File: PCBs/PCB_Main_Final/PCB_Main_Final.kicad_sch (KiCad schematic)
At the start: 0 parts

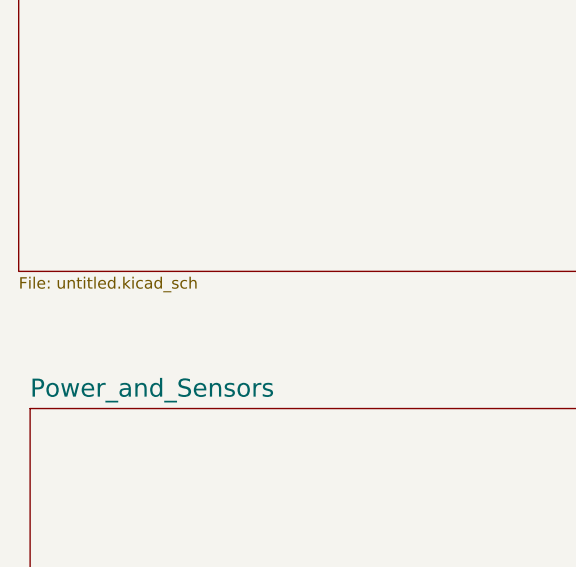
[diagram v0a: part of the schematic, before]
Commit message: fixed vias and expanded boost converter
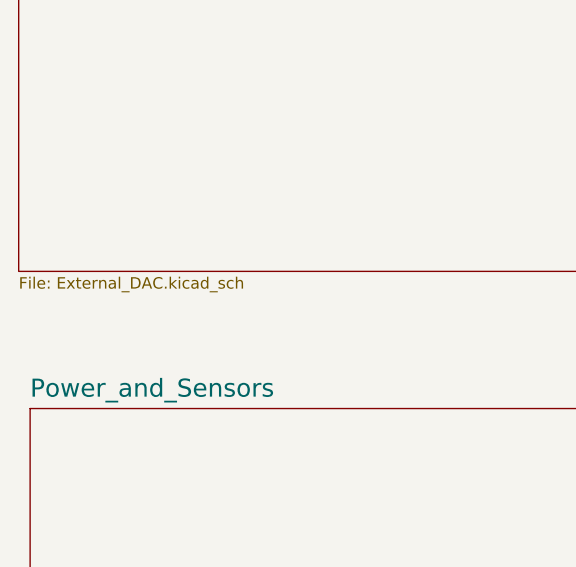
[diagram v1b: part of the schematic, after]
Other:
- sheet External_DAC: file untitled.kicad_sch -> External_DAC.kicad_sch
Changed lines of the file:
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@@
       (effects (font (size 2 2)) (justify left bottom))
     )
-    (property "Sheetfile" "untitled.kicad_sch" (at 41.91 125.0446 0)
+    (property "Sheetfile" "External_DAC.kicad_sch" (at 41.91 125.0446 0)
       (effects (font (size 1.27 1.27)) (justify left top))
     )
